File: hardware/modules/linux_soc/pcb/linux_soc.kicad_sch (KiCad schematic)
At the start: 1 part

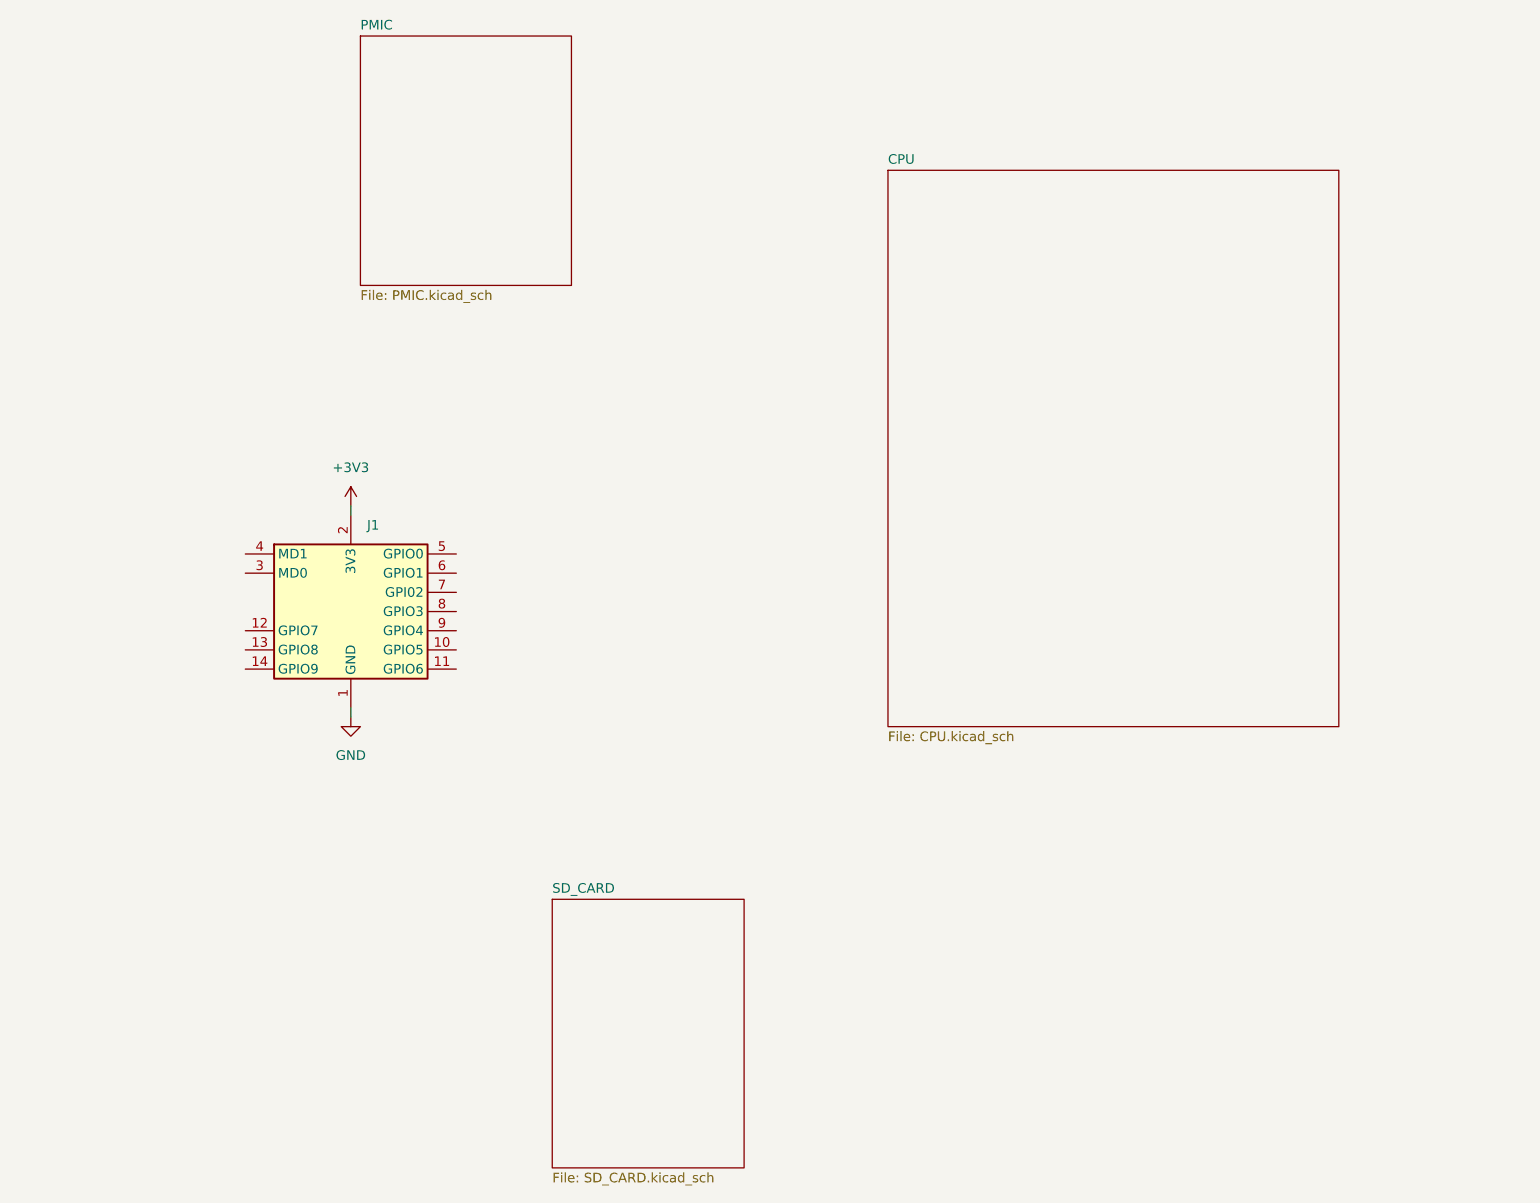
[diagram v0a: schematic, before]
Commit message: Started on PCB layout finished schematic
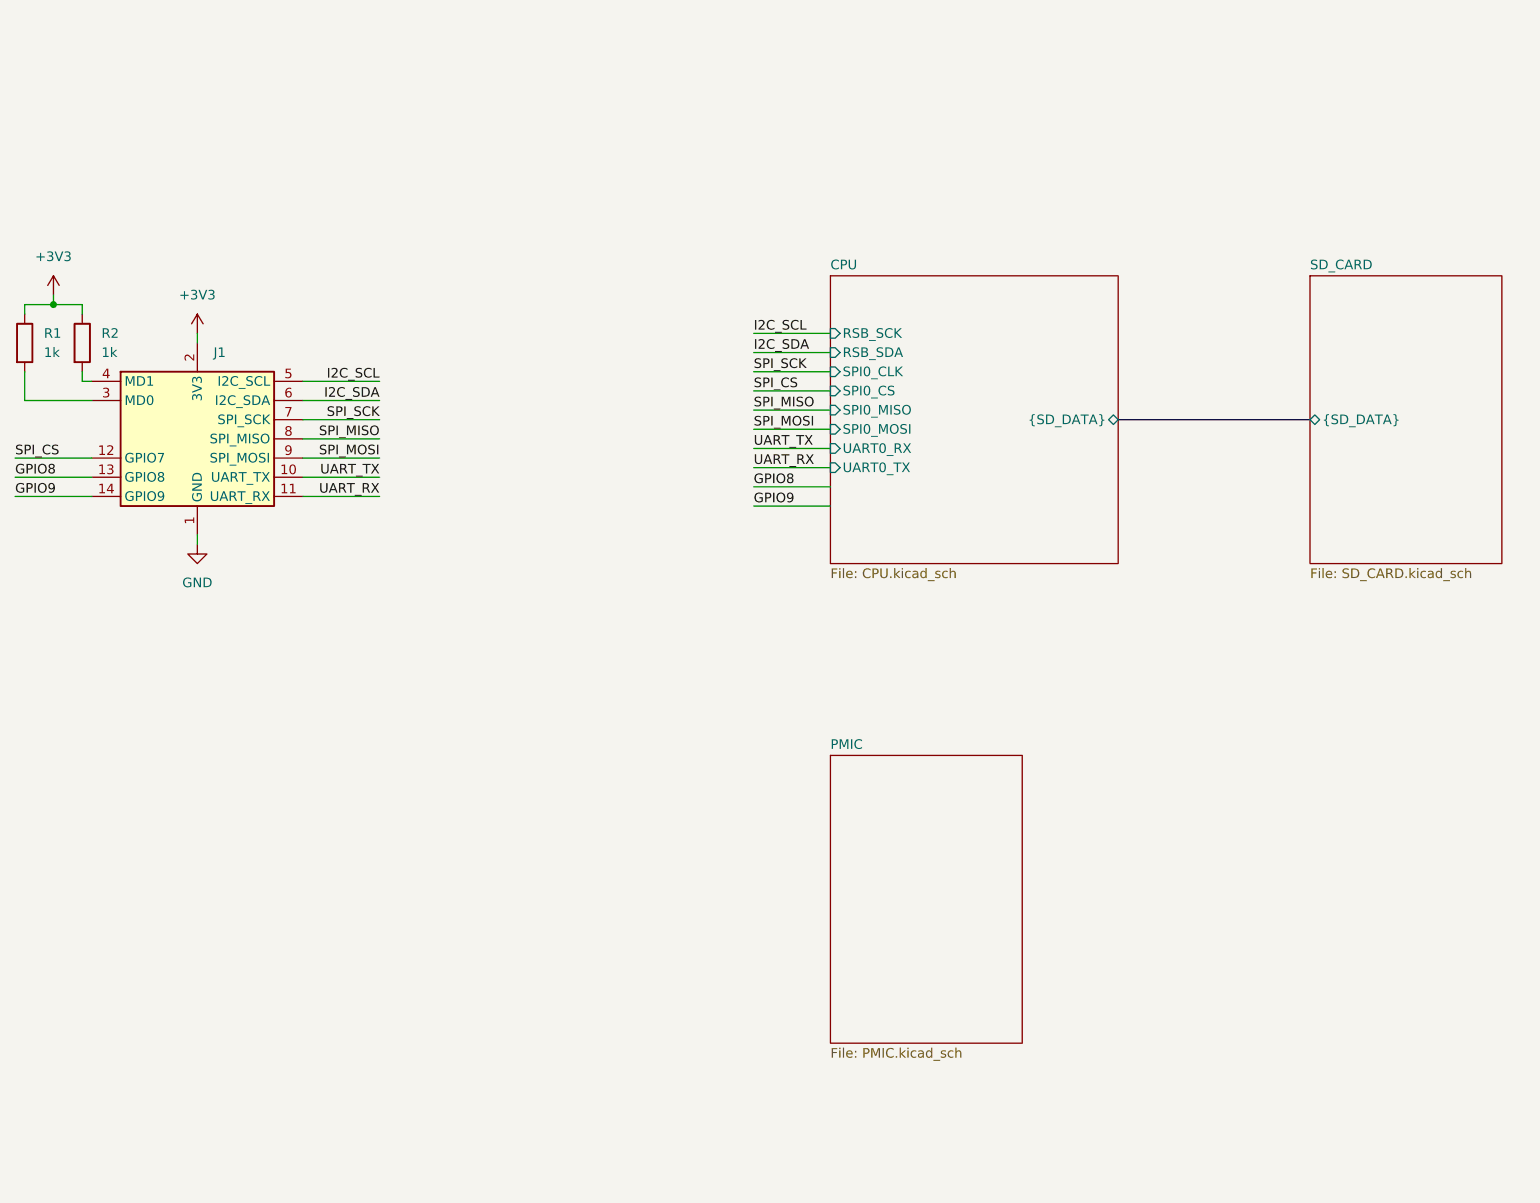
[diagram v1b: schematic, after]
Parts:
- added R1, R2: 1k, Resistor_SMD:R_0402_1005Metric, symbol Device:R
- J1: LCSC# (none) -> C706888
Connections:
- net +3V3: now also R1.1, R2.1
- net UART_TX: now reaches J1.10 (GPIO5)
- net UART_RX: now reaches J1.11 (GPIO6)
- net SPI_CS: now reaches J1.12 (GPIO7)
- net GPIO8: now reaches J1.13 (GPIO8)
- net GPIO9: now reaches J1.14 (GPIO9)
- net at J1.3 (MD0): now also R1.2
- net at J1.4 (MD1): now also R2.2
- net I2C_SCL: now reaches J1.5 (GPIO0)
- net I2C_SDA: now reaches J1.6 (GPIO1)
- net SPI_SCK: now reaches J1.7 (GPI02)
- net SPI_MISO: now reaches J1.8 (GPIO3)
- net SPI_MOSI: now reaches J1.9 (GPIO4)
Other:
- sheet CPU ports: added RSB_SCK, RSB_SDA, SPI0_CLK, SPI0_CS, SPI0_MISO, SPI0_MOSI, UART0_RX, UART0_TX, {SD_DATA}; removed none
- sheet SD_CARD ports: added {SD_DATA}; removed none
- moved on the sheet: J1
